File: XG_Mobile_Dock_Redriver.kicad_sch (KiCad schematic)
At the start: 94 parts, among them J1 5-1775443-8, J13 39301240, J14 I2C1, J2 20455-040E-76, J3 20455-040E-76, J5 USB_C_Receptacle, J6 455860005, J7 10147430-113T0LF, SW1 SW_Push, U1 DS320PR810NJXR, U2 DS320PR810NJXR

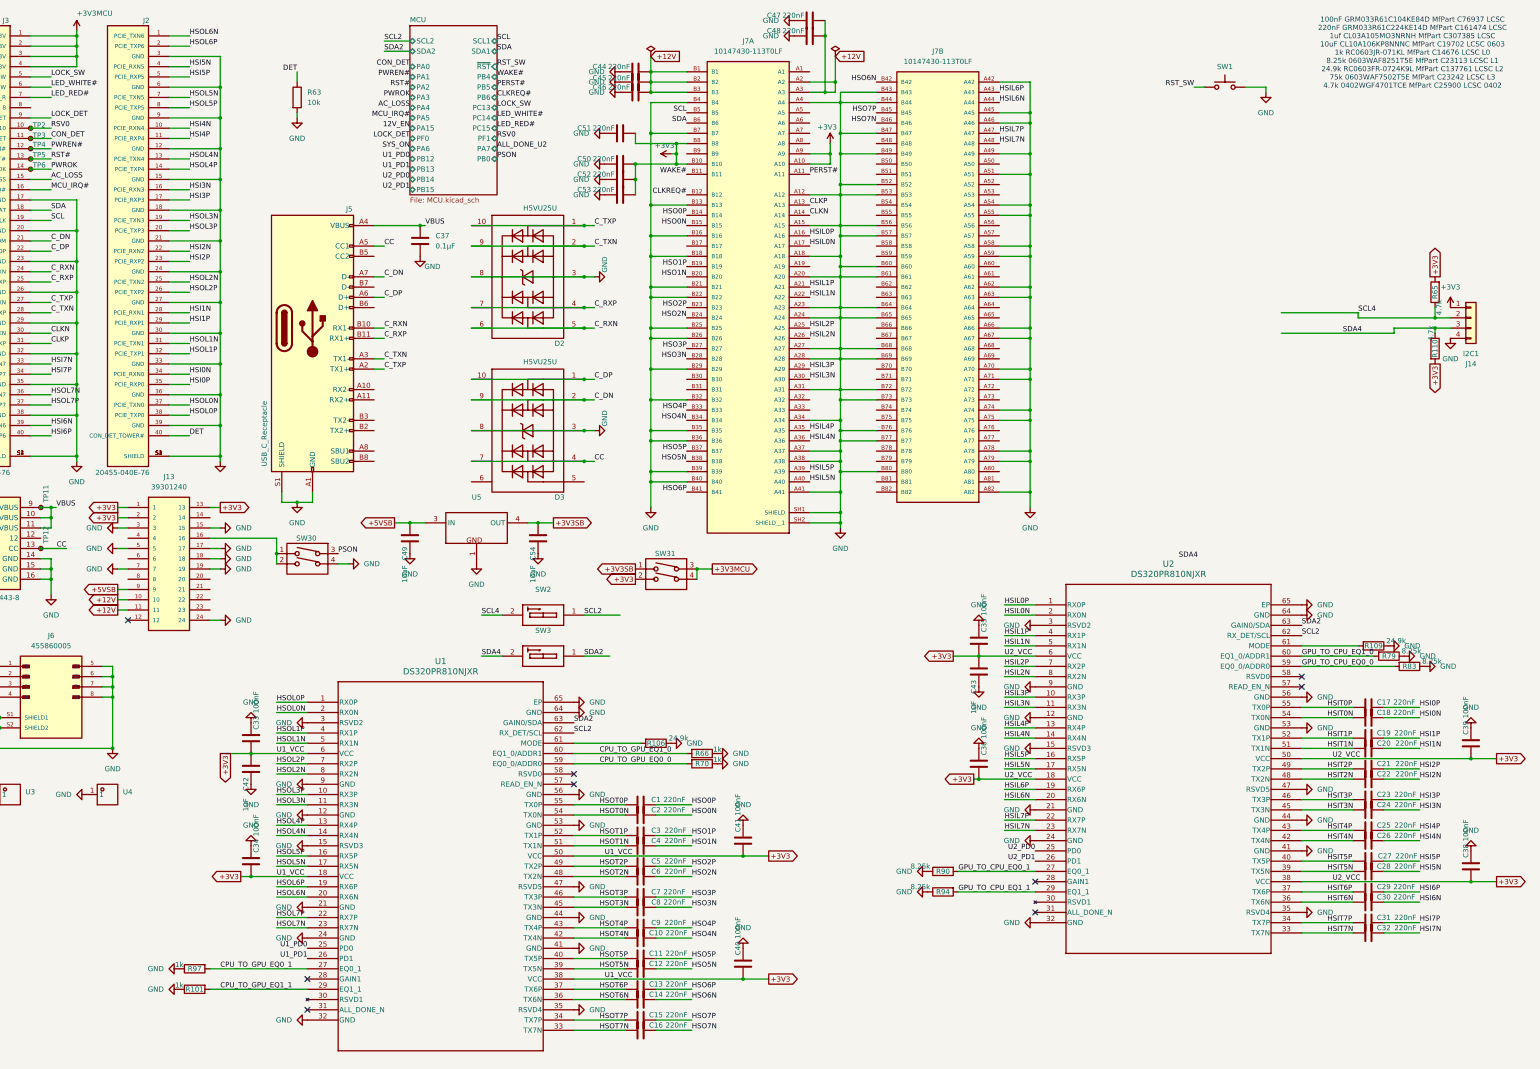
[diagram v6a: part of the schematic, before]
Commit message: added better connector for pcie slot
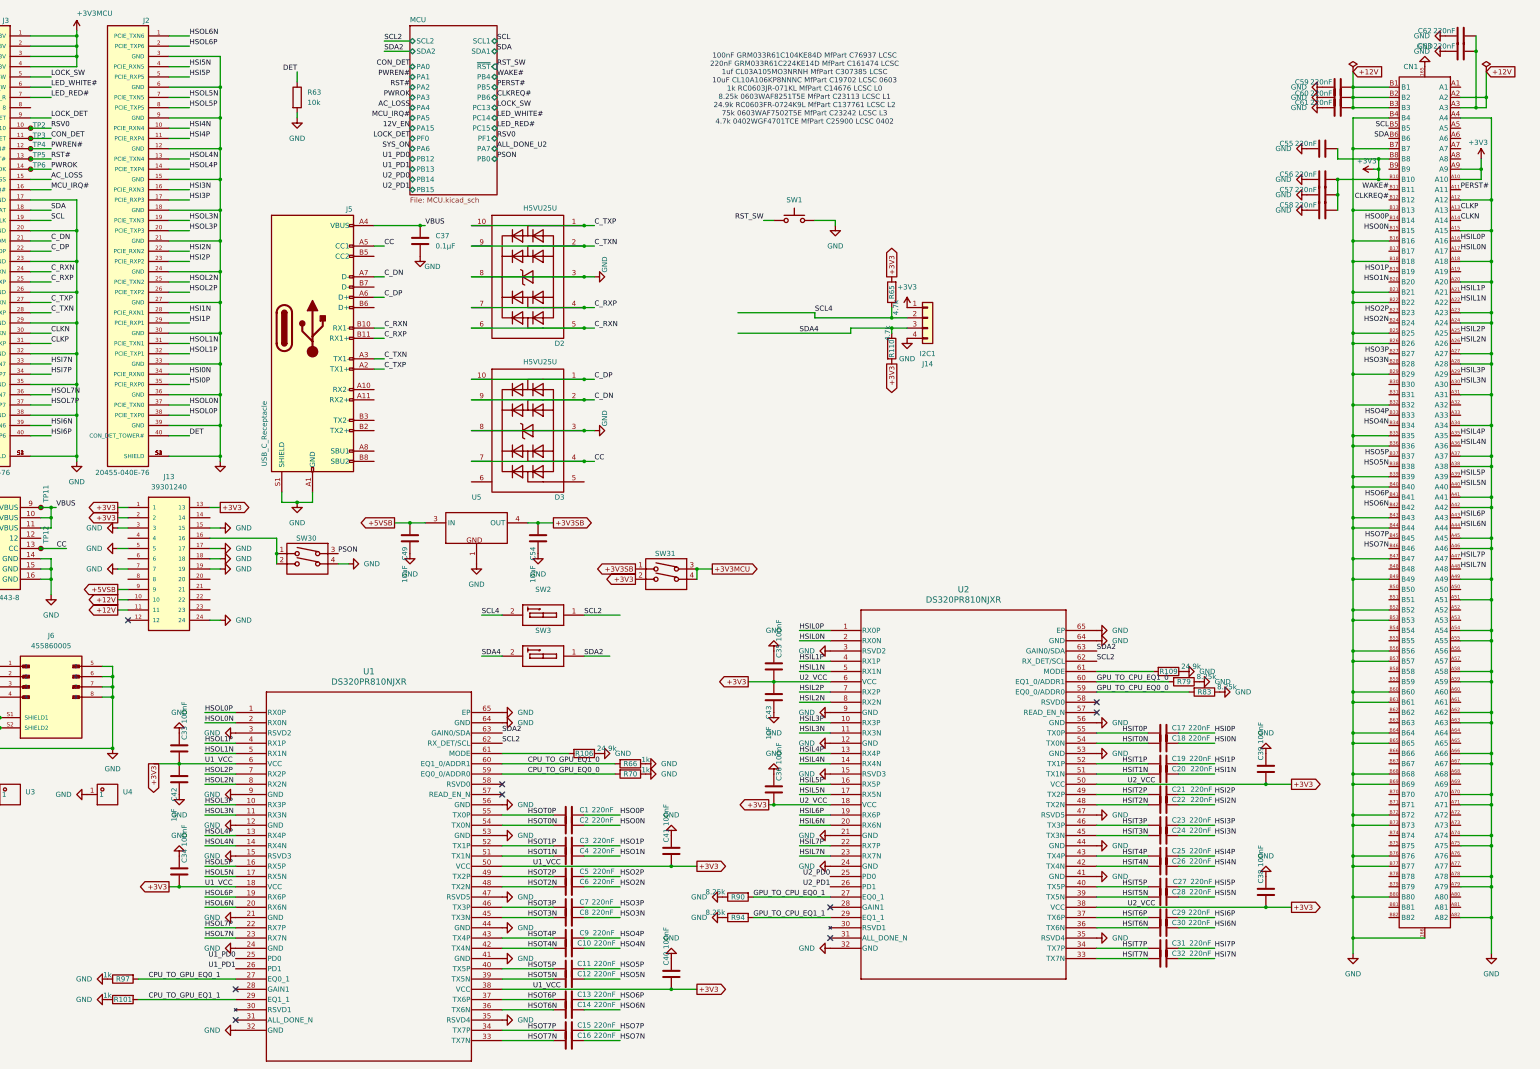
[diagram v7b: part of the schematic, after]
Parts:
- removed C44, C45, C46, C47, C48, C50, C51, C52, C53: 220nF, Capacitor_SMD:C_0201_0603Metric, symbol Device:C
- removed J7: 10147430-113T0LF, 10147430-113T0LF:AMPHENOL_10147430-113T0LF, symbol 10147430-113T0LF:10147430-113T0LF
- added C55, C56, C57, C58, C59, C60, C61, C62, C63: 220nF, Capacitor_SMD:C_0201_0603Metric, symbol Device:C
- added CN1: ~, 21650-11013T:CONN-SMD_164P-P1.00_2EH5827-D29BN-3H, symbol 21650-11013T:21650-11013T
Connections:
- net +12V: now also C59.1, C60.1, C61.1, C62.1, C63.1, CN1.A2, CN1.A3, CN1.B1, CN1.B2, CN1.B3
- net +3V3: now also C55.1, C56.1, C57.1, C58.1, CN1.A10, CN1.A9, CN1.B10, CN1.B8
- net CLKN: now also CN1.A14
- net CLKP: now also CN1.A13
- net CLKREQ#: now also CN1.B12
- net GND: now also C55.2, C56.2, C57.2, C58.2, C59.2, C60.2, C61.2, C62.2, C63.2, CN1.165, CN1.166, CN1.A12, CN1.A15, CN1.A18, CN1.A20, CN1.A23, CN1.A24, CN1.A27, CN1.A28, CN1.A31, CN1.A34, CN1.A37, CN1.A38, CN1.A4, CN1.A41, CN1.A42, CN1.A45, CN1.A46, CN1.A49, CN1.A51, CN1.A54, CN1.A55, CN1.A58, CN1.A59, CN1.A62, CN1.A63, CN1.A66, CN1.A67, CN1.A70, CN1.A71, CN1.A74, CN1.A75, CN1.A78, CN1.A79, CN1.A82, CN1.B13, CN1.B16, CN1.B18, CN1.B21, CN1.B22, CN1.B25, CN1.B26, CN1.B29, CN1.B32, CN1.B35, CN1.B36, CN1.B39, CN1.B4, CN1.B40, CN1.B43, CN1.B44, CN1.B47, CN1.B49, CN1.B52, CN1.B53, CN1.B56, CN1.B57, CN1.B60, CN1.B61, CN1.B64, CN1.B65, CN1.B68, CN1.B69, CN1.B7, CN1.B72, CN1.B73, CN1.B76, CN1.B77, CN1.B80
- net HSIL0N: now also CN1.A17
- net HSIL0P: now also CN1.A16
- net HSIL1N: now also CN1.A22
- net HSIL1P: now also CN1.A21
- net HSIL2N: now also CN1.A26
- net HSIL2P: now also CN1.A25
- net HSIL3N: now also CN1.A30
- net HSIL3P: now also CN1.A29
- net HSIL4N: now also CN1.A36
- net HSIL4P: now also CN1.A35
- net HSIL5N: now also CN1.A40
- net HSIL5P: now also CN1.A39
- net HSIL6N: now also CN1.A44
- net HSIL6P: now also CN1.A43
- net HSIL7N: now also CN1.A48
- net HSIL7P: now also CN1.A47
- net HSO0N: now also CN1.B15
- net HSO0P: now also CN1.B14
- net HSO1N: now also CN1.B20
- net HSO1P: now also CN1.B19
- net HSO2N: now also CN1.B24
- net HSO2P: now also CN1.B23
- net HSO3N: now also CN1.B28
- net HSO3P: now also CN1.B27
- net HSO4N: now also CN1.B34
- net HSO4P: now also CN1.B33
- net HSO5N: now also CN1.B38
- net HSO5P: now also CN1.B37
- net HSO6N: now also CN1.B42
- net HSO6P: now also CN1.B41
- net HSO7N: now also CN1.B46
- net HSO7P: now also CN1.B45
- net PERST#: now also CN1.A11
- net SCL: now also CN1.B5
- net SDA: now also CN1.B6
- net WAKE#: now also CN1.B11
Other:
- moved on the sheet: C1, C10, C11, C12, C13, C14, C15, C16, C17, C18, C19, C2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

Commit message: fixed part number
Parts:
- CN1: LCSC (none) -> C22464457; LCSC Part Name PCIE5.0 卡边缘连接器 PCI-E5.0 PCIE连接器 SMT 带ECB接地总线 立贴 -> (none); Manufacturer UMaxconn(友贸) -> (none); Manufacturer Part 21650-11013T -> (none); Part_Number (none) -> 21650-11013T; Supplier LCSC -> (none); Supplier Part C22464457 -> (none)
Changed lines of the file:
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@@
 			)
 		)
-		(property "Manufacturer Part" "21650-11013T"
+		(property "Part_Number" "21650-11013T"
 			(at 381 134.62 0)
 			(effects
@@
 			)
 		)
-		(property "Manufacturer" "UMaxconn(友贸)"
+		(property "LCSC" "C22464457"
 			(at 381 134.62 0)
 			(effects
-				(font
-					(size 1.27 1.27)
-				)
-				(hide yes)
-			)
-		)
-		(property "Supplier Part" "C22464457"
-			(at 381 134.62 0)
-			(effects
-				(font
-					(size 1.27 1.27)
-				)
-				(hide yes)
-			)
-		)
-		(property "Supplier" "LCSC"
-			(at 381 134.62 0)
-			(effects
-				(font
-					(size 1.27 1.27)
-				)
-				(hide yes)
-			)
-		)
-		(property "LCSC Part Name" "PCIE5.0 卡边缘连接器 PCI-E5.0 PCIE连接器 SMT 带ECB接地总线 立贴"
-			(at 381 134.62 0)
-			(effects
